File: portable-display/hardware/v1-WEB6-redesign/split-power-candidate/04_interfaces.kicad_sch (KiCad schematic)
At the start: 42 parts, among them J4 KD024EGOIN152-01, J5 MicroSD, Q3 AO3401A, SW1 UP, SW2 DOWN, SW3 OK, SW4 BACK, U10 TPS65631DPDR, U8 TPS22918DBVR

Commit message: fix: resolve screen RESET/TE level matching
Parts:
- added R32: 10k, Sameat:0402, symbol Sameat:R32_10k
- R20: value 100k -> 10k; symbol Sameat:R20_100k -> Sameat:R20_10k
- R21: value 10k -> 100; symbol Sameat:R21_10k -> Sameat:R21_100
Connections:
- net 3V3: no longer R20.1
- net GND: now also R20.1, R32.2
- net LCD_RST: now also R32.1
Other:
- note added: "DISPLAY GPIO: PA8 (U2.66) -> LCD_RST; PA9 / EINT9 (U2.65) <- LCD_TE. Both use 1V8. R32 10k holds reset LOW at boot. R29 must remain fitted 0R; VDDIO must share the PA supply. Update firmware pin assignments; PD19 / PD20 are now unconnected. See DISPLAY_IO_REPAIR_CN.md."
- note added: "TF POWER: R20 10k to GND; R21 100R. PH12 / SD_PWR_EN: LOW or Hi-Z = ON, HIGH = OFF. 3V3 must be valid before boot. Card detection / cold-start waveforms still require hardware validation."
- moved on the sheet: C29, C30, C31, C42, C43, C44, C45, C46, C47, C48, C49, C50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

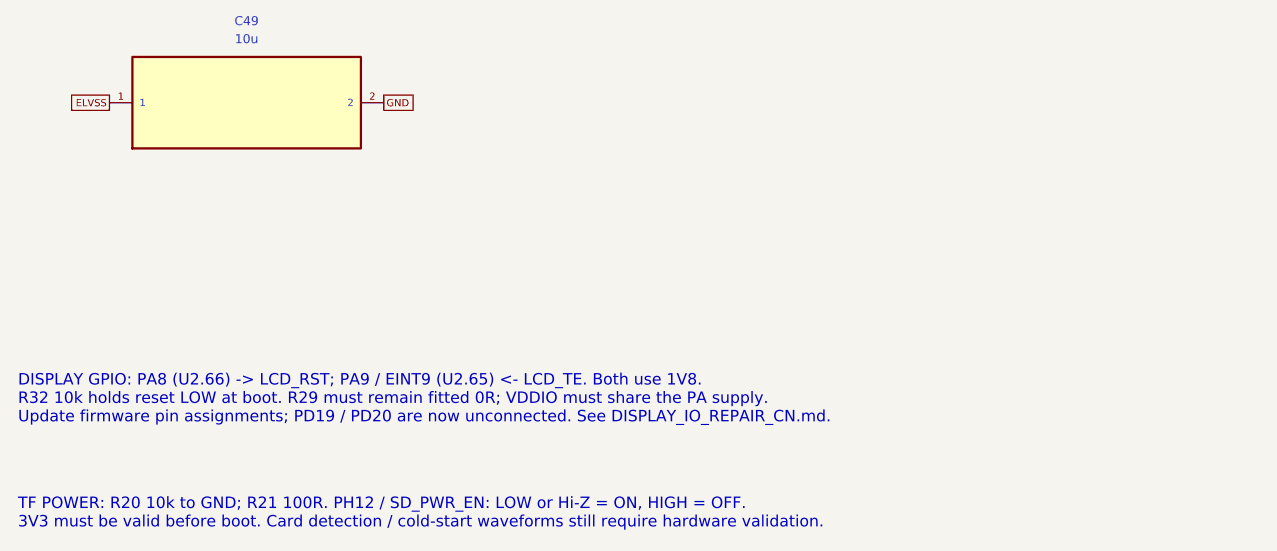
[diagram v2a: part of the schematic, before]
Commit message: fix: repair USB routing by swapping DP/DM pins on U9 and updating layout files
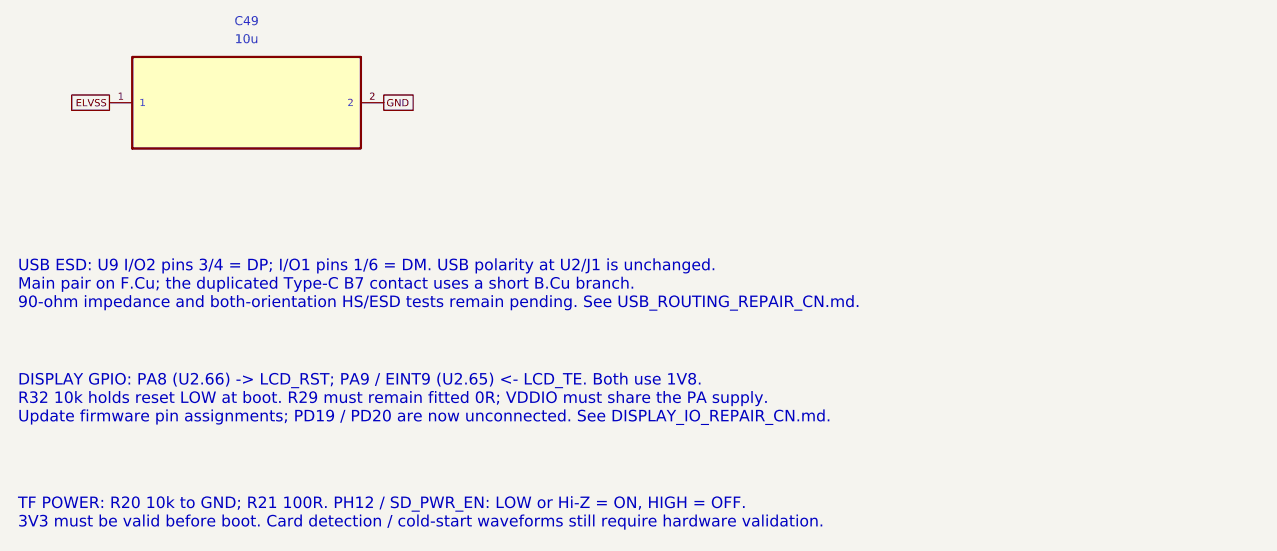
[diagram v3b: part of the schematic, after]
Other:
- note added: "USB ESD: U9 I/O2 pins 3/4 = DP; I/O1 pins 1/6 = DM. USB polarity at U2/J1 is unchanged. Main pair on F.Cu; the duplicated Type-C B7 contact uses a short B.Cu branch. 90-ohm impedance and both-orientation HS/ESD tests remain pending. See USB_ROUTING_REPAIR_CN.md."
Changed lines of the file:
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@@
 	(title_block
 		(title "04 Display / SD / Buttons")
-		(date "2026-10-01")
-		(rev "WAKE1")
+		(date "2026-10-02")
+		(rev "USB1")
 		(company "Sameat")
 		(comment 1 "Current PCB pin nets; C3036461 factory configuration NOT verified")
@@
 	)
 	(embedded_fonts no)
+	(text "USB ESD: U9 I/O2 pins 3/4 = DP; I/O1 pins 1/6 = DM. USB polarity at U2/J1 is unchanged.\nMain pair on F.Cu; the duplicated Type-C B7 contact uses a short B.Cu branch.\n90-ohm impedance and both-orientation HS/ESD tests remain pending. See USB_ROUTING_REPAIR_CN.md."
+		(at 38.1 345.44 0)
+		(effects
+			(font
+				(size 1.27 1.27)
+			)
+			(justify left)
+		)
+	)
 	(text "TF POWER: R20 10k to GND; R21 100R. PH12 / SD_PWR_EN: LOW or Hi-Z = ON, HIGH = OFF.\n3V3 must be valid before boot. Card detection / cold-start waveforms still require hardware validation."
 		(at 38.1 370.84 0)

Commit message: fix(pcb): replace D6-D14 with ESDLC5V0LB (C20168172) on dedicated DFN1006-2 land
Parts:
- D10: value PESD4V0 -> ESDLC5V0LB; footprint Sameat:0402 -> Sameat:DFN1006-2; symbol Sameat:D10_PESD4V0 -> Sameat:D10_ESDLC5V0LB; LCSC (none) -> C20168172; MPN PESD4V0Y1BBSF -> ESDLC5V0LB
- D11: value PESD4V0 -> ESDLC5V0LB; footprint Sameat:0402 -> Sameat:DFN1006-2; symbol Sameat:D11_PESD4V0 -> Sameat:D11_ESDLC5V0LB; LCSC (none) -> C20168172; MPN PESD4V0Y1BBSF -> ESDLC5V0LB
- D12: value PESD4V0 -> ESDLC5V0LB; footprint Sameat:0402 -> Sameat:DFN1006-2; symbol Sameat:D12_PESD4V0 -> Sameat:D12_ESDLC5V0LB; LCSC (none) -> C20168172; MPN PESD4V0Y1BBSF -> ESDLC5V0LB
- D6: value PESD4V0 -> ESDLC5V0LB; footprint Sameat:0402 -> Sameat:DFN1006-2; symbol Sameat:D6_PESD4V0 -> Sameat:D6_ESDLC5V0LB; LCSC (none) -> C20168172; MPN PESD4V0Y1BBSF -> ESDLC5V0LB
- D7: value PESD4V0 -> ESDLC5V0LB; footprint Sameat:0402 -> Sameat:DFN1006-2; symbol Sameat:D7_PESD4V0 -> Sameat:D7_ESDLC5V0LB; LCSC (none) -> C20168172; MPN PESD4V0Y1BBSF -> ESDLC5V0LB
- D8: value PESD4V0 -> ESDLC5V0LB; footprint Sameat:0402 -> Sameat:DFN1006-2; symbol Sameat:D8_PESD4V0 -> Sameat:D8_ESDLC5V0LB; LCSC (none) -> C20168172; MPN PESD4V0Y1BBSF -> ESDLC5V0LB
- D9: value PESD4V0 -> ESDLC5V0LB; footprint Sameat:0402 -> Sameat:DFN1006-2; symbol Sameat:D9_PESD4V0 -> Sameat:D9_ESDLC5V0LB; LCSC (none) -> C20168172; MPN PESD4V0Y1BBSF -> ESDLC5V0LB
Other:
- moved on the sheet: C29, C30, C31, C43, C44, C45, C47, C51, D10, D11, D12, D5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

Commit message: feat(j5): swap microSD to in-stock XKTF-0803-0, TPD4E05U06 flow-through ESD, reroute SD bus off Y1
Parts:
- removed D10: ESDLC5V0LB, Sameat:DFN1006-2, symbol Sameat:D10_ESDLC5V0LB
- removed D11: ESDLC5V0LB, Sameat:DFN1006-2, symbol Sameat:D11_ESDLC5V0LB
- removed D12: ESDLC5V0LB, Sameat:DFN1006-2, symbol Sameat:D12_ESDLC5V0LB
- removed D6: ESDLC5V0LB, Sameat:DFN1006-2, symbol Sameat:D6_ESDLC5V0LB
- removed D7: ESDLC5V0LB, Sameat:DFN1006-2, symbol Sameat:D7_ESDLC5V0LB
- removed D8: ESDLC5V0LB, Sameat:DFN1006-2, symbol Sameat:D8_ESDLC5V0LB
- removed D9: ESDLC5V0LB, Sameat:DFN1006-2, symbol Sameat:D9_ESDLC5V0LB
- added U12: TPD4E05U06DQAR, Sameat:TPD4E05U06_DQA, symbol Sameat:U12_TPD4E05U06DQAR
- added U13: TPD4E05U06DQAR, Sameat:TPD4E05U06_DQA, symbol Sameat:U13_TPD4E05U06DQAR
- J5: footprint Sameat:MICROSD -> Sameat:XKTF-0803-0; LCSC C5205359 -> C381083; MPN MUP-M617-2 -> XKTF-0803-0
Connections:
- net GND: now also U12.3 (GND), U12.8 (GND), U13.3 (GND), U13.8 (GND)
- net SD_CLK: now also U13.5 (IO4), U13.6 (NC_FT4)
- net SD_CMD: now also U12.2 (IO2), U12.9 (NC_FT2)
- net SD_D0: now also U13.4 (IO3), U13.7 (NC_FT3)
- net SD_D1: now also U13.2 (IO2), U13.9 (NC_FT2)
- net SD_D2: now also U12.5 (IO4), U12.6 (NC_FT4)
- net SD_D3: now also U12.4 (IO3), U12.7 (NC_FT3)
- net SD_DET: now also U12.1 (IO1), U12.10 (NC_FT1)
- no-connect marks 15 -> 17
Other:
- moved on the sheet: C30, C42, C44, C47, C48, C49, J5, L5, L6, Q3, R20, R22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

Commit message: fix(power): feed U10 TPS65631 from 3V3 via local In2 taps; 2x10u+100n under U10
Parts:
- C46, C47: footprint Sameat:0603 -> Sameat:0402; LCSC (none) -> C15525; MPN (none) -> CL05A106MQ5NUNC
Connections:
- net 3V3: now also C46.2, C47.2, L5.1, U10.11 (AVIN), U10.12 (PVIN)
- net GND: now also C46.1, C47.1; no longer C46.2, C47.2
- removed net VSYS: C46.1, C47.1, L5.1, U10.11 (AVIN), U10.12 (PVIN)
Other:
- moved on the sheet: C29, C30, C31, C43, C44, C45, C46, C47, C48, C49, C50, D5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
